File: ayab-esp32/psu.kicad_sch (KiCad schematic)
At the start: 48 parts, among them J602 940, Q602 BCM857BV, Q603 AO3401A, U401 XL1509, U402 XL1509

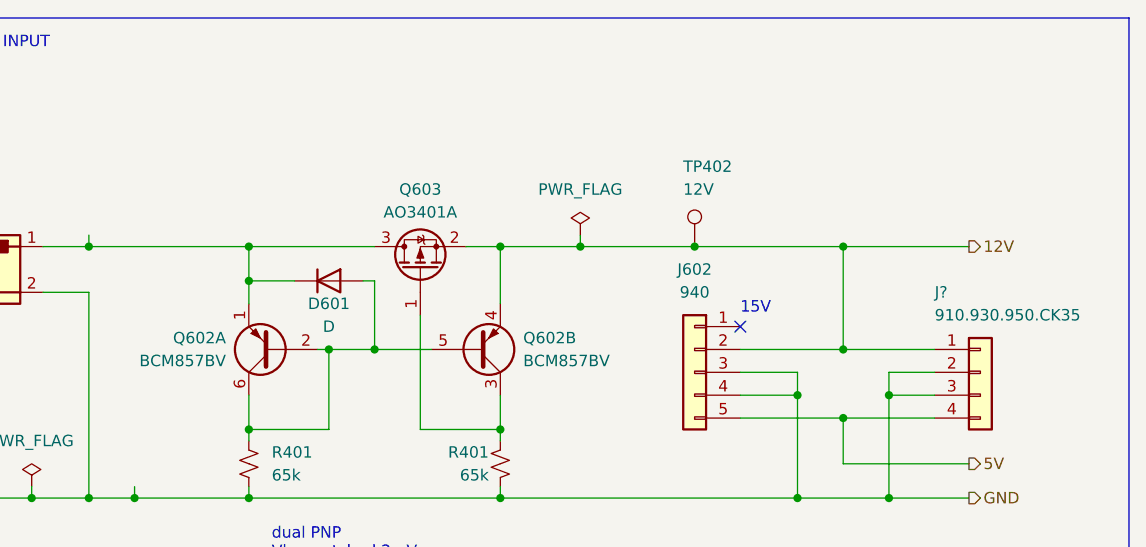
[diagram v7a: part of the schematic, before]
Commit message: refactor for i2c expander
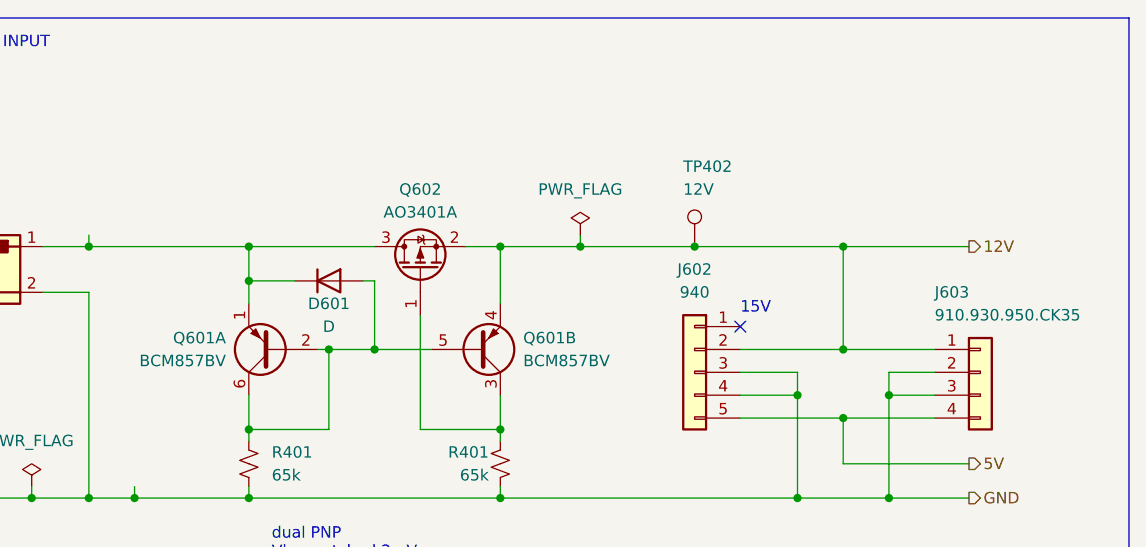
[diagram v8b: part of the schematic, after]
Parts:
- gave numbers to parts that had none: 1
- renumbered Q602 to Q601, Q603 to Q602
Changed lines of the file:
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@@
       (project "ayab-esp32"
         (path "/ad16b75f-afc8-4717-a7c6-8dd7b69a18e2/512b1de4-f8f4-4173-a7be-69b46f59a5e5"
-          (reference "R603") (unit 1)
+          (reference "R602") (unit 1)
         )
       )
@@
       (project "ayab-esp32"
         (path "/ad16b75f-afc8-4717-a7c6-8dd7b69a18e2/512b1de4-f8f4-4173-a7be-69b46f59a5e5"
-          (reference "R610") (unit 1)
+          (reference "R609") (unit 1)
         )
       )
@@
       (project "ayab-esp32"
         (path "/ad16b75f-afc8-4717-a7c6-8dd7b69a18e2/512b1de4-f8f4-4173-a7be-69b46f59a5e5"
-          (reference "R605") (unit 1)
+          (reference "R604") (unit 1)
         )
       )
@@
   (symbol (lib_id "ayab-esp32:Q_Dual_PNP_PNP_E1B1C2E2B2C1") (at 71.12 53.34 180) (unit 1)
     (in_bom yes) (on_board yes) (dnp no) (fields_autoplaced)
-    (property "Reference" "Q602" (at 66.04 52.07 0)
+    (property "Reference" "Q601" (at 66.04 52.07 0)
       (effects (font (size 1.27 1.27)) (justify left))
     )
@@
       (project "ayab-esp32"
         (path "/ad16b75f-afc8-4717-a7c6-8dd7b69a18e2/512b1de4-f8f4-4173-a7be-69b46f59a5e5"
-          (reference "Q602") (unit 1)
+          (reference "Q601") (unit 1)
         )
       )
@@
       (project "ayab-esp32"
         (path "/ad16b75f-afc8-4717-a7c6-8dd7b69a18e2/512b1de4-f8f4-4173-a7be-69b46f59a5e5"
-          (reference "R607") (unit 1)
+          (reference "R606") (unit 1)
         )
       )
@@
   (symbol (lib_id "ayab-esp32:AO3401A") (at 87.63 44.45 90) (unit 1)
     (in_bom yes) (on_board yes) (dnp no) (fields_autoplaced)
-    (property "Reference" "Q603" (at 87.63 35.56 90)
+    (property "Reference" "Q602" (at 87.63 35.56 90)
       (effects (font (size 1.27 1.27)))
     )
@@
       (project "ayab-esp32"
         (path "/ad16b75f-afc8-4717-a7c6-8dd7b69a18e2/512b1de4-f8f4-4173-a7be-69b46f59a5e5"
-          (reference "Q603") (unit 1)
+          (reference "Q602") (unit 1)
         )
       )
@@
       (project "ayab-esp32"
         (path "/ad16b75f-afc8-4717-a7c6-8dd7b69a18e2/512b1de4-f8f4-4173-a7be-69b46f59a5e5"
-          (reference "R604") (unit 1)
+          (reference "R603") (unit 1)
         )
       )
@@
       (project "ayab-esp32"
         (path "/ad16b75f-afc8-4717-a7c6-8dd7b69a18e2/512b1de4-f8f4-4173-a7be-69b46f59a5e5"
-          (reference "R602") (unit 1)
+          (reference "R601") (unit 1)
         )
       )
@@
       (project "ayab-esp32"
         (path "/ad16b75f-afc8-4717-a7c6-8dd7b69a18e2/512b1de4-f8f4-4173-a7be-69b46f59a5e5"
-          (reference "R608") (unit 1)
+          (reference "R607") (unit 1)
         )
       )
@@
   (symbol (lib_id "ayab-esp32:Conn_01x04") (at 149.86 55.88 0) (unit 1)
     (in_bom yes) (on_board yes) (dnp no)
-    (property "Reference" "J?" (at 144.78 46.99 0)
+    (property "Reference" "J603" (at 144.78 46.99 0)
       (effects (font (size 1.27 1.27)) (justify left))
     )
@@
       (project "ayab-esp32"
         (path "/ad16b75f-afc8-4717-a7c6-8dd7b69a18e2/512b1de4-f8f4-4173-a7be-69b46f59a5e5"
-          (reference "J?") (unit 1)
+          (reference "J603") (unit 1)
         )
       )
@@
   (symbol (lib_id "ayab-esp32:Q_Dual_PNP_PNP_E1B1C2E2B2C1") (at 93.98 53.34 0) (mirror x) (unit 2)
     (in_bom yes) (on_board yes) (dnp no) (fields_autoplaced)
-    (property "Reference" "Q602" (at 99.06 52.07 0)
+    (property "Reference" "Q601" (at 99.06 52.07 0)
       (effects (font (size 1.27 1.27)) (justify left))
     )
@@
       (project "ayab-esp32"
         (path "/ad16b75f-afc8-4717-a7c6-8dd7b69a18e2/512b1de4-f8f4-4173-a7be-69b46f59a5e5"
-          (reference "Q602") (unit 2)
+          (reference "Q601") (unit 2)
         )
       )
@@
       (project "ayab-esp32"
         (path "/ad16b75f-afc8-4717-a7c6-8dd7b69a18e2/512b1de4-f8f4-4173-a7be-69b46f59a5e5"
-          (reference "R606") (unit 1)
+          (reference "R605") (unit 1)
         )
       )
@@
       (project "ayab-esp32"
         (path "/ad16b75f-afc8-4717-a7c6-8dd7b69a18e2/512b1de4-f8f4-4173-a7be-69b46f59a5e5"
-          (reference "R609") (unit 1)
-        )
-      )
+          (reference "R608") (unit 1)
+        )
+      )
